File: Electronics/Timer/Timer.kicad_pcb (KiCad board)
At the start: 2 copper layers, 110 x 44.6 mm, 24 parts, among them CN1 RJ12-UNSHLD, U1 MIC5504-3.3YM5, U2 74HC165

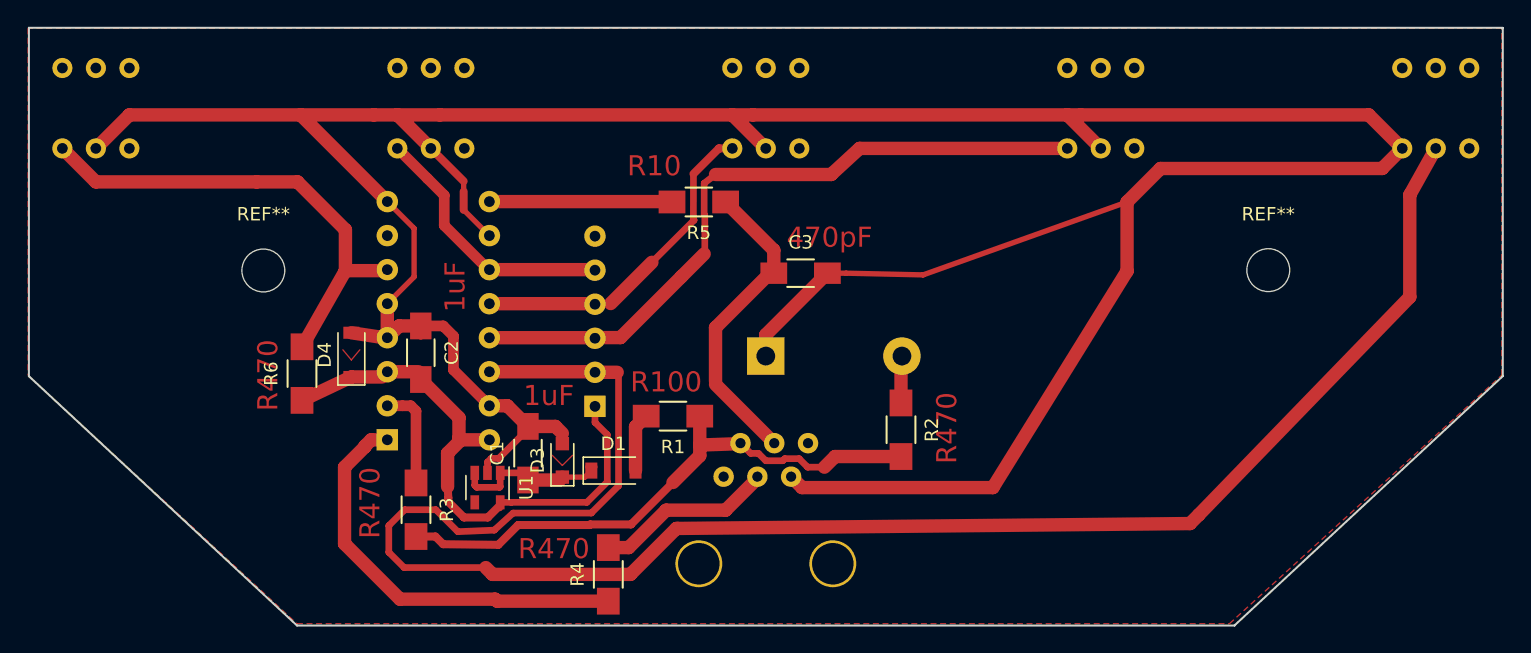
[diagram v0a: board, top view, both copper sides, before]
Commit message: Corrected design error in Timer board, updated routing.
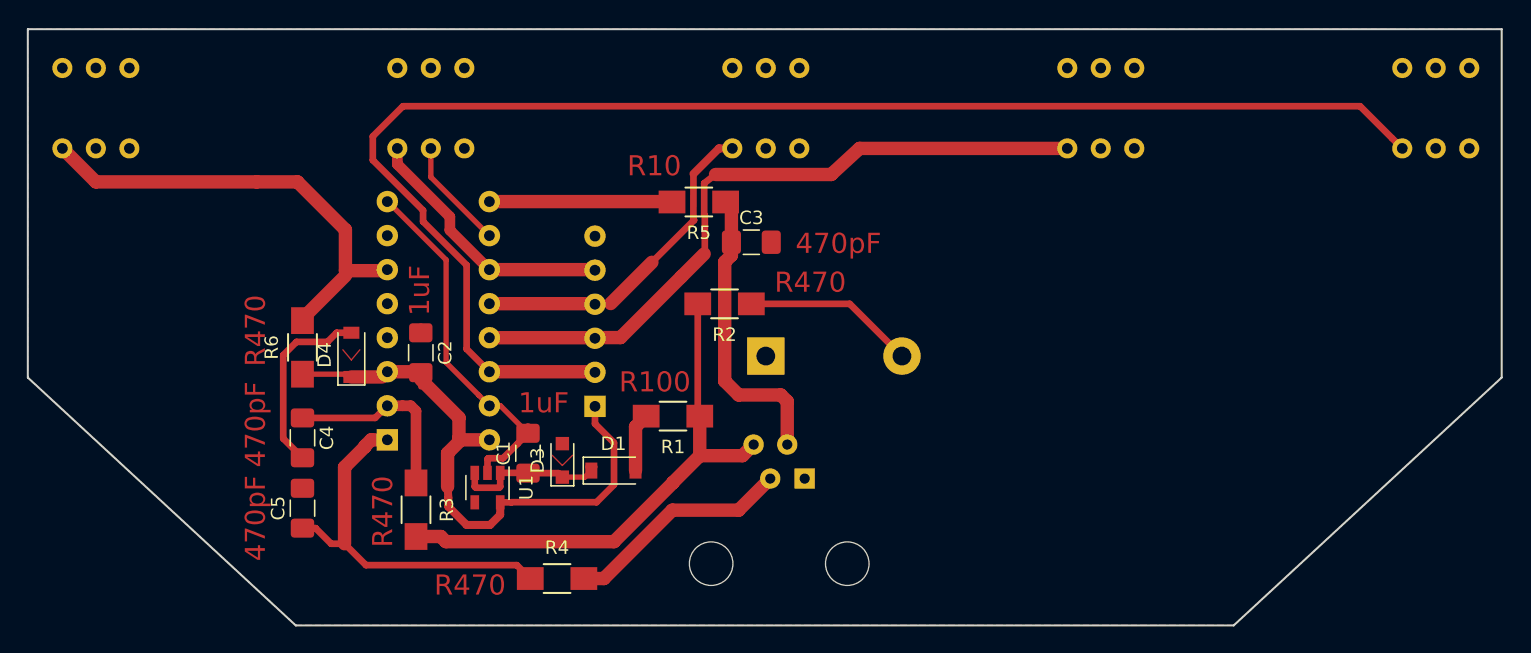
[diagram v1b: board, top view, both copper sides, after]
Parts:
- removed CN1: RJ12-UNSHLD, PiKwonDo:TH-RJ12
- removed REF** (x2): MountingHole_3.2mm_M3, MountingHole:MountingHole_3.2mm_M3
- added C4: 470pF, Capacitor_SMD:C_1206_3216Metric_Pad1.42x1.75mm_HandSolder, F.Cu at (65.4, 164.5)
- added C5: 470pF, Capacitor_SMD:C_1206_3216Metric_Pad1.42x1.75mm_HandSolder, F.Cu at (65.4, 169.7)
- added J1: RJ10, Timer:RJ14, B.Cu at (104.2, 165.0)
- C1, C2, C3: footprint Capacitors_SMD:C_1206_HandSoldering -> Capacitor_SMD:C_1206_3216Metric_Pad1.42x1.75mm_HandSolder
- moved R2 16.2 mm to (96.9, 154.5), turned to 180 degrees
- moved C3 4.34 mm to (98.9, 149.9)
- moved R4 3.84 mm to (84.4, 175.0), turned to 0 degrees
- moved R6 1.95 mm to (65.4, 157.7)
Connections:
- S4 pad 1: GND -> Net-(RN1-Pad2)
- S4 pad 2: Net-(RN1-Pad2) -> GND
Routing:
- net GND: track 261.2 -> 51.9 mm
- net Net-(RN1-Pad2): track 137.7 -> 108.6 mm
- net Net-(D2-Pad2): track 3.53 -> 13.0 mm
- net /CLK: track 7.67 -> 14.4 mm
- net Net-(J1-Pad4): track 43.5 -> 39.8 mm
- net Net-(J1-Pad3): track 13.5 -> 17.0 mm
- net /~LOAD~: track 31.3 -> 28.4 mm
- net +3V3: track 44.4 -> 46.0 mm
- net Net-(R6-Pad2): track 36.4 -> 34.9 mm
- net Net-(C3-Pad1): track 23.5 -> 22.3 mm
- net +5V: track 12.8 -> 11.9 mm
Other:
- board size 110 x 44.6 mm -> 110 x 44.5 mm
- net class 1mm: clearance 0.3 -> 0.31; via_dia 0.6 -> 1.1; via_drill 0.4 -> 0.8
- net class Default: clearance 0.3 -> 0.31; trace_width 0.4 -> 0.5; via_dia 0.6 -> 1.1; via_drill 0.4 -> 0.8
- rule trace_clearance: 0.3 -> 0.31

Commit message: Updated trace routing and board outline. Added mounting holes.
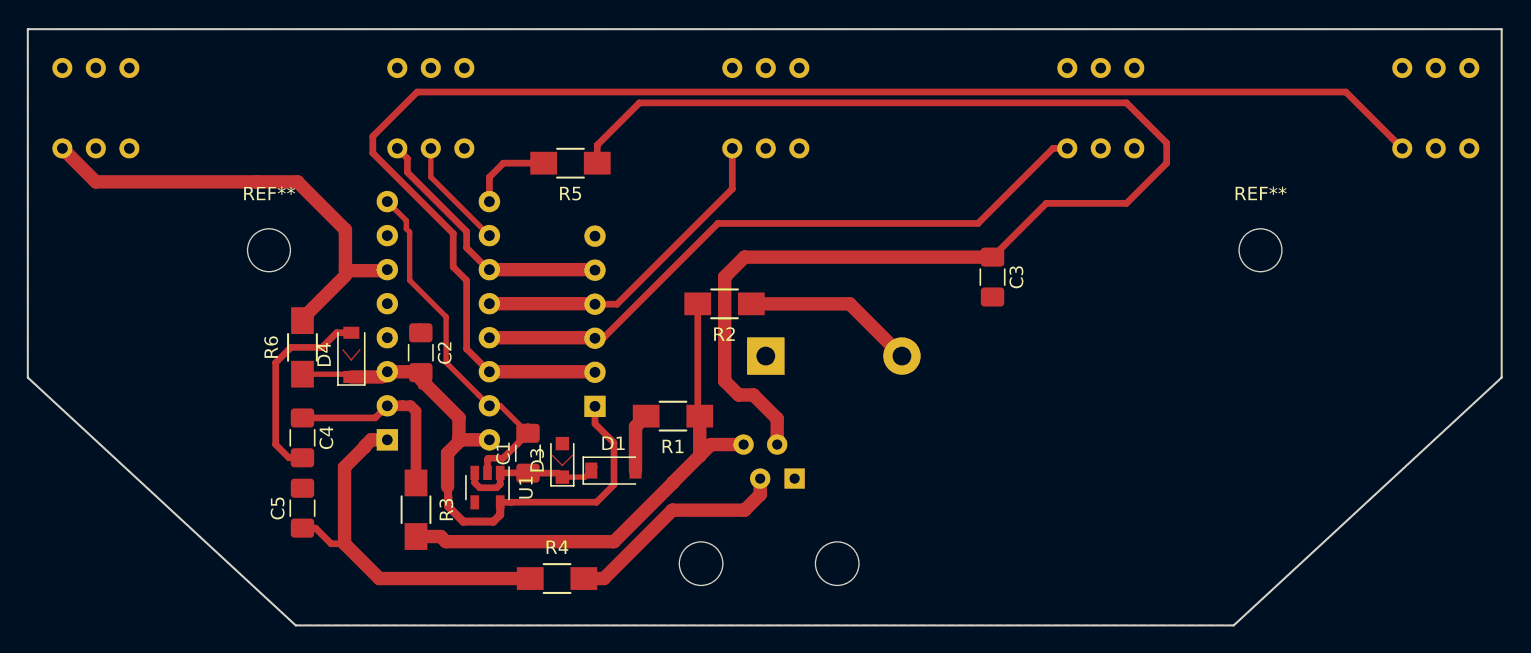
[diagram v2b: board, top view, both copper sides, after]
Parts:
- added REF**: MountingHole_3.2mm_M3, MountingHole:MountingHole_3.2mm_M3, F.Cu at (136.9, 150.5)
- added REF**: MountingHole_3.2mm_M3, MountingHole:MountingHole_3.2mm_M3, F.Cu at (62.9, 150.5)
- moved C3 18.2 mm to (116.9, 152.5), turned to 270 degrees
- moved R5 10.0 mm to (85.4, 144.0)
- moved J1 0.75 mm to (103.4, 165.0)
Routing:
- net Net-(C3-Pad1): track 22.3 -> 99.2 mm
- net /Q: track 13.6 -> 6.30 mm
- net Net-(RN1-Pad3): track 52.6 -> 49.6 mm
- net GND: track 51.9 -> 52.9 mm
- net Net-(RN1-Pad2): track 108.6 -> 109.5 mm
- net Net-(J1-Pad4): track 39.8 -> 39.0 mm
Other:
- board text removed: "1uF"
- board text removed: "470pF"
- board text removed: "R10"
- board text removed: "R100"
- board text removed: "R470"

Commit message: Updated boards for two-sided manufacture.
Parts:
- removed REF** (x2): MountingHole_3.2mm_M3, MountingHole:MountingHole_3.2mm_M3
- added M3: MountingHole_3.2mm_M3, MountingHole:MountingHole_3.2mm_M3, F.Cu at (62.8, 150.4)
- added M3: MountingHole_3.2mm_M3, MountingHole:MountingHole_3.2mm_M3, F.Cu at (136.9, 150.6)
- D1: footprint Diodes_SMD:D_SOD-123 -> Diode_SMD:D_SMA_Handsoldering
- moved D1 1.80 mm to (90.4, 166.7)
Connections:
- RN1 pad 6: Net-(RN1-Pad6) -> (no net)
- S1 pad 3: Net-(S1-Pad3) -> (no net)
- S2 pad 3: Net-(S2-Pad3) -> (no net)
- S3 pad 3: Net-(S3-Pad3) -> (no net)
- S4 pad 3: Net-(S4-Pad3) -> (no net)
- S5 pad 3: Net-(S5-Pad3) -> (no net)
- U1 pad 4: Net-(U1-Pad4) -> (no net)
- U2 pad 7: Net-(U2-Pad7) -> (no net)
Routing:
- net GND: track 52.9 -> 59.3 mm
- net (no net): track 4.14 -> 0.00 mm
- net +3V3: track 45.8 -> 48.4 mm
- net +5V: track 11.7 -> 13.7 mm
- net Net-(J1-Pad4): track 39.0 -> 40.4 mm
- net Net-(C3-Pad1): track 99.2 -> 98.2 mm
- net Net-(RN1-Pad3): track 49.6 -> 49.0 mm
- added copper zone on B.Cu, net GND
- removed copper zone on F.Cu, net GND
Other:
- board text added: "PiKwonDo Timer Board Version 1.0 David Wright 2020"

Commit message: Updated component sourcing
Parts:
- removed M3 (x2): MountingHole_3.2mm_M3, MountingHole:MountingHole_3.2mm_M3
- removed R6: 470, Resistors_SMD:R_1206_HandSoldering
- moved C5 3.27 mm to (67.3, 167.1), turned to 180 degrees
- moved C4 2.24 mm to (67.3, 163.3), turned to 180 degrees
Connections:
- RN1 pad 6: (no net) -> Net-(RN1-Pad6)
- S5 pad 1: Net-(R6-Pad2) -> Net-(RN1-Pad6)
- U2 pad 6: Net-(R6-Pad2) -> Net-(RN1-Pad6)
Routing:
- net Net-(RN1-Pad6): track 0.00 -> 205.2 mm
- net Net-(R6-Pad2): track 34.9 -> 0.00 mm
- net +3V3: track 48.4 -> 43.5 mm
- net GND: track 59.3 -> 54.5 mm
- net /~LOAD~: track 28.4 -> 24.2 mm
- net /CLK: track 14.3 -> 11.1 mm
- net Net-(C3-Pad1): track 98.2 -> 97.4 mm
